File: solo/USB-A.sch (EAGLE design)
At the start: 23 parts, among them U1 USB_TRACES

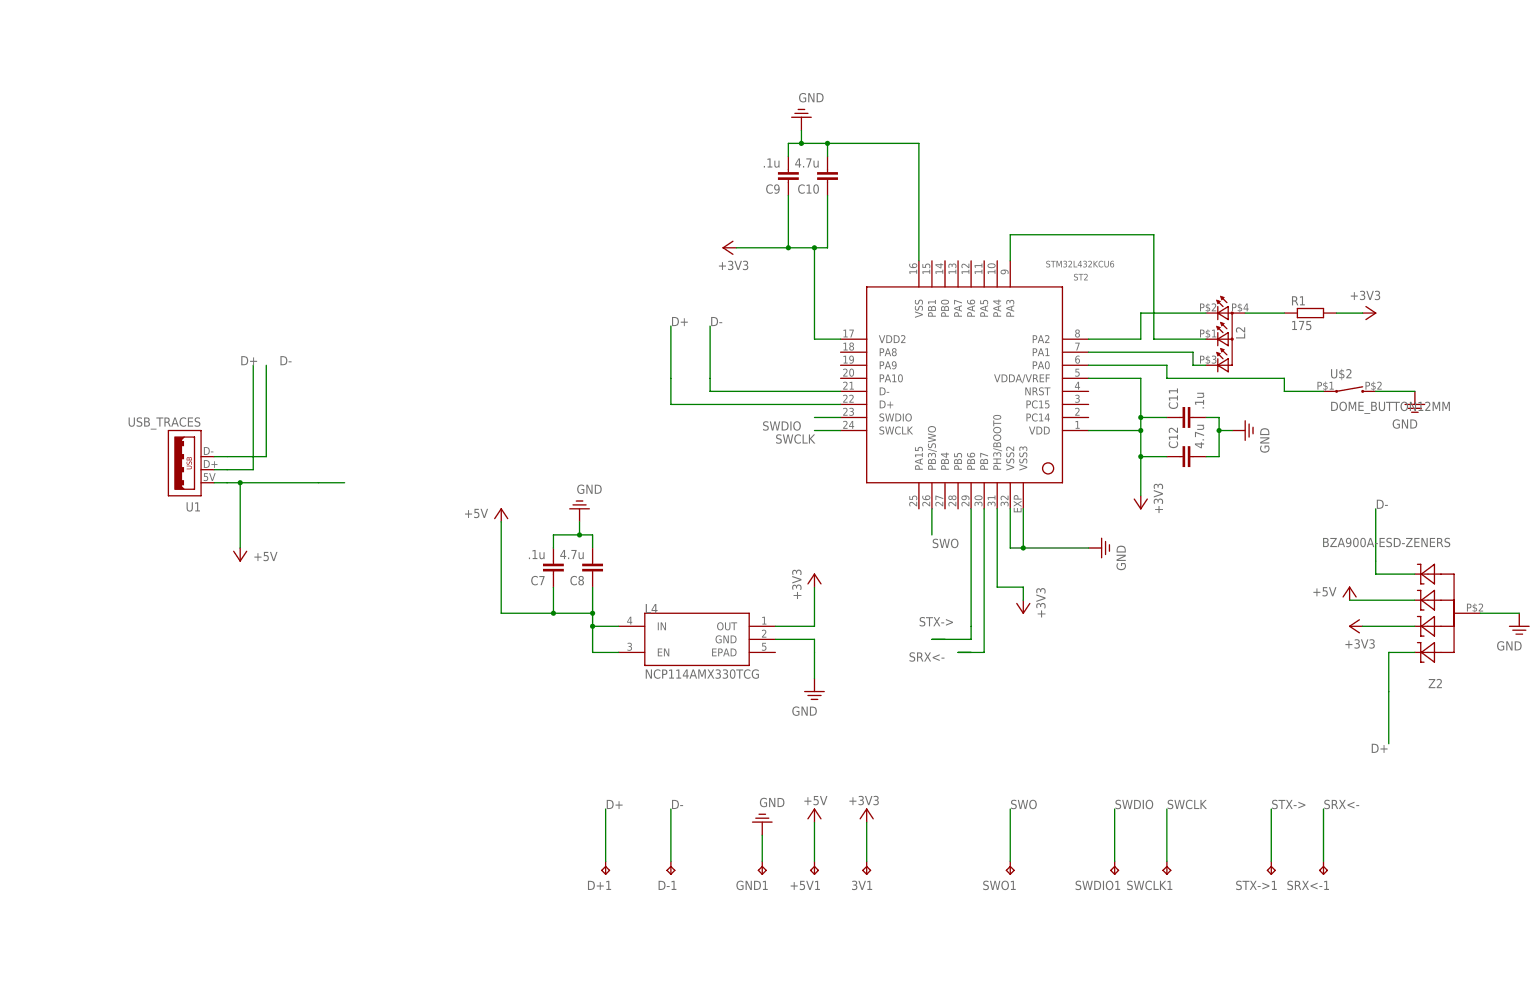
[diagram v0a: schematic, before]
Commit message: fix AMS part footprint :(
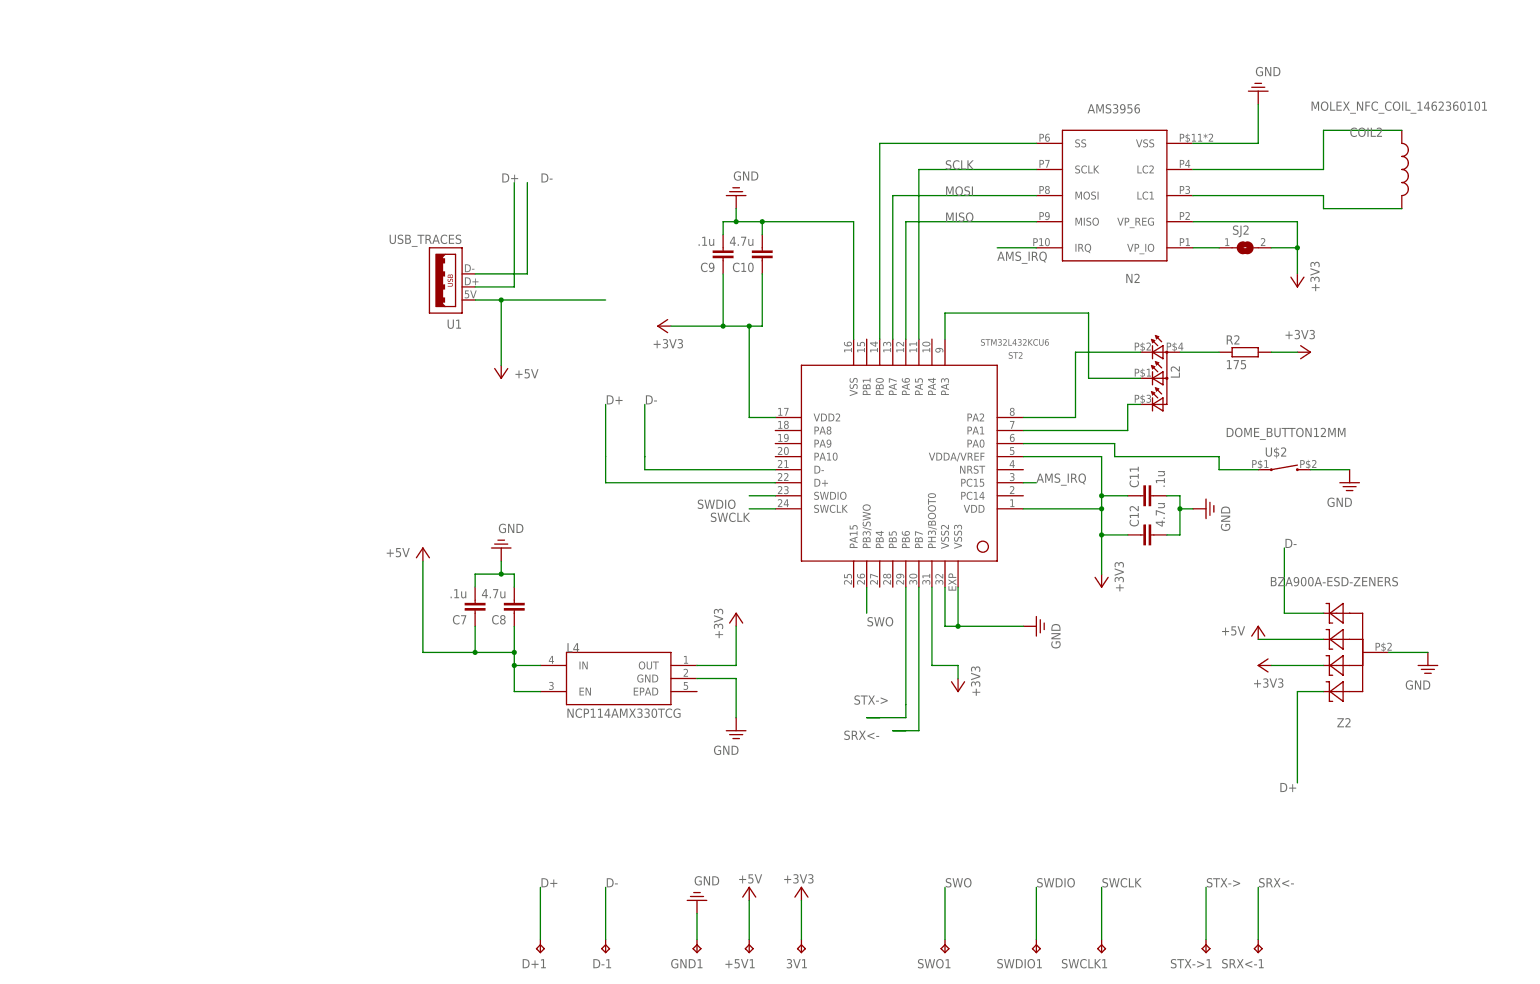
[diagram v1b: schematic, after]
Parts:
- removed R1: 175, efm-fido:RESISTOR
- added COIL2: MOLEX_NFC_COIL_1462360101, efm-fido:MOLEX_NFC_COIL_1462360101
- added N2: AMS3956, efm-fido:AMS3956
- added R2: 175, efm-fido:RESISTOR
- added SJ2: (no value), jumper:SJ
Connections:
- removed net N$7: L2.A2, R1.1
- new net AMS_CS: N2.SS, ST2.PB0
- new net AMS_IRQ: N2.IRQ, ST2.PC15
- new net MISO: N2.MISO, ST2.PA6
- new net MOSI: N2.MOSI, ST2.PA7
- new net N$15: L2.A2, R2.1
- new net N$23: N2.VP_IO, SJ2.1
- new net N$25: COIL2.1, N2.LC2
- new net N$26: COIL2.2, N2.LC1
- new net SCLK: N2.SCLK, ST2.PA5
- net +3V3: now also N2.VP_REG, R2.2, SJ2.2; no longer R1.2
- net PE: now also N2.VSS
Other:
- moved on the sheet: +5V1, 3V1, C10, C11, C12, C7, C8, C9, D+1, D-1, GND1, L2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

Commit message: use hatched footprints, remove bridge
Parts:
- removed SJ2: (no value), jumper:SJ
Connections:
- removed net N$23: N2.VP_IO, SJ2.1
- net +3V3: now also N2.VP_IO; no longer SJ2.2
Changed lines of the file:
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@@
 <part name="+3V14" library="supply1" library_urn="urn:adsk.eagle:library:371" deviceset="+3V3" device=""/>
 <part name="+3V15" library="supply1" library_urn="urn:adsk.eagle:library:371" deviceset="+3V3" device=""/>
-<part name="U$2" library="efm-fido" library_urn="urn:adsk.eagle:library:4245354" deviceset="DOME_BUTTON" device="12MM" package3d_urn="urn:adsk.eagle:package:5648519/5"/>
-<part name="N2" library="efm-fido" library_urn="urn:adsk.eagle:library:4245354" deviceset="AMS3956" device="" package3d_urn="urn:adsk.eagle:package:5825738/3"/>
+<part name="U$2" library="efm-fido" library_urn="urn:adsk.eagle:library:4245354" deviceset="DOME_BUTTON" device="12MM" package3d_urn="urn:adsk.eagle:package:5648519/7"/>
+<part name="N2" library="efm-fido" library_urn="urn:adsk.eagle:library:4245354" deviceset="AMS3956" device="" package3d_urn="urn:adsk.eagle:package:5825738/4"/>
 <part name="SUPPLY18" library="supply2" library_urn="urn:adsk.eagle:library:372" deviceset="PE" device="" value="GND"/>
 <part name="+3V16" library="supply1" library_urn="urn:adsk.eagle:library:371" deviceset="+3V3" device=""/>
-<part name="SJ2" library="jumper" library_urn="urn:adsk.eagle:library:252" deviceset="SJ" device="" package3d_urn="urn:adsk.eagle:package:15471/1"/>
 <part name="COIL2" library="efm-fido" library_urn="urn:adsk.eagle:library:4245354" deviceset="MOLEX_NFC_COIL_1462360101" device="" package3d_urn="urn:adsk.eagle:package:7114966/5"/>
 </parts>
@@
 <instance part="+3V16" gate="G$1" x="292.1" y="134.62" smashed="yes" rot="R180">
 <attribute name="VALUE" x="294.64" y="139.7" size="1.778" layer="96" rot="R270"/>
-</instance>
-<instance part="SJ2" gate="1" x="281.94" y="142.24" smashed="yes">
-<attribute name="NAME" x="279.4" y="144.78" size="1.778" layer="95"/>
-<attribute name="VALUE" x="279.4" y="138.43" size="1.778" layer="96"/>
 </instance>
 <instance part="COIL2" gate="G$1" x="312.42" y="157.48" smashed="yes">
@@
 <pinref part="+3V16" gate="G$1" pin="+3V3"/>
 <wire x1="292.1" y1="137.16" x2="292.1" y2="142.24" width="0.1524" layer="91"/>
-<pinref part="SJ2" gate="1" pin="2"/>
 <wire x1="292.1" y1="142.24" x2="292.1" y2="147.32" width="0.1524" layer="91"/>
-<wire x1="287.02" y1="142.24" x2="292.1" y2="142.24" width="0.1524" layer="91"/>
 <junction x="292.1" y="142.24"/>
+<pinref part="N2" gate="G$1" pin="VP_IO"/>
+<wire x1="271.78" y1="142.24" x2="292.1" y2="142.24" width="0.1524" layer="91"/>
 </segment>
 </net>
@@
 </segment>
 </net>
-<net name="N$23" class="0">
-<segment>
-<pinref part="SJ2" gate="1" pin="1"/>
-<pinref part="N2" gate="G$1" pin="VP_IO"/>
-<wire x1="276.86" y1="142.24" x2="271.78" y2="142.24" width="0.1524" layer="91"/>
-</segment>
-</net>

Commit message: prep for nfc
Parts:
- removed COIL2: MOLEX_NFC_COIL_1462360101, efm-fido:MOLEX_NFC_COIL_1462360101
- added C2, C3, MID: .1u, efm-fido:CAPACITOR
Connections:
- net N$25: now also C2.1, MID.2; no longer COIL2.1
- net N$26: now also C3.2, MID.1; no longer COIL2.2
- net PE: now also C2.2, C3.1
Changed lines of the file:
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@@
 <part name="C12" library="efm-fido" library_urn="urn:adsk.eagle:library:4245354" deviceset="CAPACITOR" device="" package3d_urn="urn:adsk.eagle:package:4245806/7" value="4.7u"/>
 <part name="SUPPLY16" library="supply2" library_urn="urn:adsk.eagle:library:372" deviceset="PE" device="" value="GND"/>
-<part name="ST2" library="efm-fido" library_urn="urn:adsk.eagle:library:4245354" deviceset="STM32L432KCU6" device="" package3d_urn="urn:adsk.eagle:package:4245373/6"/>
+<part name="ST2" library="efm-fido" library_urn="urn:adsk.eagle:library:4245354" deviceset="STM32L432KCU6" device="" package3d_urn="urn:adsk.eagle:package:4245373/7"/>
 <part name="SWO1" library="efm-fido" library_urn="urn:adsk.eagle:library:4245354" deviceset="TEST_POINT" device="" package3d_urn="urn:adsk.eagle:package:4245792/4"/>
 <part name="L4" library="efm-fido" library_urn="urn:adsk.eagle:library:4245354" deviceset="NCP114AMX330TCG" device="" package3d_urn="urn:adsk.eagle:package:5621121/3"/>
@@
 <part name="SUPPLY18" library="supply2" library_urn="urn:adsk.eagle:library:372" deviceset="PE" device="" value="GND"/>
 <part name="+3V16" library="supply1" library_urn="urn:adsk.eagle:library:371" deviceset="+3V3" device=""/>
-<part name="COIL2" library="efm-fido" library_urn="urn:adsk.eagle:library:4245354" deviceset="MOLEX_NFC_COIL_1462360101" device="" package3d_urn="urn:adsk.eagle:package:7114966/5"/>
+<part name="MID" library="efm-fido" library_urn="urn:adsk.eagle:library:4245354" deviceset="CAPACITOR" device="" package3d_urn="urn:adsk.eagle:package:4245806/7" value=".1u"/>
+<part name="C2" library="efm-fido" library_urn="urn:adsk.eagle:library:4245354" deviceset="CAPACITOR" device="" package3d_urn="urn:adsk.eagle:package:4245806/7" value=".1u"/>
+<part name="C3" library="efm-fido" library_urn="urn:adsk.eagle:library:4245354" deviceset="CAPACITOR" device="" package3d_urn="urn:adsk.eagle:package:4245806/7" value=".1u"/>
+<part name="SUPPLY1" library="supply2" library_urn="urn:adsk.eagle:library:372" deviceset="PE" device="" value="GND"/>
+<part name="SUPPLY2" library="supply2" library_urn="urn:adsk.eagle:library:372" deviceset="PE" device="" value="GND"/>
 </parts>
 <sheets>
@@
 <attribute name="VALUE" x="294.64" y="139.7" size="1.778" layer="96" rot="R270"/>
 </instance>
-<instance part="COIL2" gate="G$1" x="312.42" y="157.48" smashed="yes">
-<attribute name="NAME" x="302.26" y="163.83" size="1.778" layer="95"/>
-<attribute name="VALUE" x="294.64" y="168.91" size="1.778" layer="96"/>
+<instance part="MID" gate="G$1" x="314.96" y="157.48" smashed="yes" rot="R180">
+<attribute name="NAME" x="313.436" y="157.099" size="1.778" layer="95" rot="R180"/>
+<attribute name="VALUE" x="313.436" y="162.179" size="1.778" layer="96" rot="R180"/>
+</instance>
+<instance part="C2" gate="G$1" x="314.96" y="172.72" smashed="yes" rot="R180">
+<attribute name="NAME" x="313.436" y="172.339" size="1.778" layer="95" rot="R180"/>
+<attribute name="VALUE" x="313.436" y="177.419" size="1.778" layer="96" rot="R180"/>
+</instance>
+<instance part="C3" gate="G$1" x="317.5" y="142.24" smashed="yes" rot="R180">
+<attribute name="NAME" x="315.976" y="141.859" size="1.778" layer="95" rot="R180"/>
+<attribute name="VALUE" x="315.976" y="146.939" size="1.778" layer="96" rot="R180"/>
+</instance>
+<instance part="SUPPLY1" gate="PE" x="317.5" y="134.62" smashed="yes">
+<attribute name="VALUE" x="313.055" y="129.921" size="1.778" layer="96"/>
+</instance>
+<instance part="SUPPLY2" gate="PE" x="314.96" y="182.88" smashed="yes" rot="R180">
+<attribute name="VALUE" x="319.405" y="187.579" size="1.778" layer="96" rot="R180"/>
 </instance>
 </instances>
@@
 <pinref part="SUPPLY18" gate="PE" pin="PE"/>
 </segment>
+<segment>
+<pinref part="C2" gate="G$1" pin="2"/>
+<pinref part="SUPPLY2" gate="PE" pin="PE"/>
+<wire x1="314.96" y1="177.8" x2="314.96" y2="180.34" width="0.1524" layer="91"/>
+</segment>
+<segment>
+<pinref part="C3" gate="G$1" pin="1"/>
+<pinref part="SUPPLY1" gate="PE" pin="PE"/>
+<wire x1="317.5" y1="139.7" x2="317.5" y2="137.16" width="0.1524" layer="91"/>
+</segment>
 </net>
 <net name="+3V3" class="0">
@@
 <wire x1="271.78" y1="157.48" x2="297.18" y2="157.48" width="0.1524" layer="91"/>
 <wire x1="297.18" y1="157.48" x2="297.18" y2="165.1" width="0.1524" layer="91"/>
-<pinref part="COIL2" gate="G$1" pin="1"/>
-<wire x1="297.18" y1="165.1" x2="312.42" y2="165.1" width="0.1524" layer="91"/>
+<wire x1="297.18" y1="165.1" x2="314.96" y2="165.1" width="0.1524" layer="91"/>
+<pinref part="MID" gate="G$1" pin="2"/>
+<wire x1="314.96" y1="162.56" x2="314.96" y2="165.1" width="0.1524" layer="91"/>
+<pinref part="C2" gate="G$1" pin="1"/>
+<wire x1="314.96" y1="170.18" x2="314.96" y2="165.1" width="0.1524" layer="91"/>
+<junction x="314.96" y="165.1"/>
 </segment>
 </net>
@@
 <wire x1="271.78" y1="152.4" x2="297.18" y2="152.4" width="0.1524" layer="91"/>
 <wire x1="297.18" y1="152.4" x2="297.18" y2="149.86" width="0.1524" layer="91"/>
-<pinref part="COIL2" gate="G$1" pin="2"/>
-<wire x1="297.18" y1="149.86" x2="312.42" y2="149.86" width="0.1524" layer="91"/>
-</segment>
-</net>
+<wire x1="297.18" y1="149.86" x2="314.96" y2="149.86" width="0.1524" layer="91"/>
+<pinref part="MID" gate="G$1" pin="1"/>
+<wire x1="314.96" y1="149.86" x2="314.96" y2="154.94" width="0.1524" layer="91"/>
+<pinref part="C3" gate="G$1" pin="2"/>
+<wire x1="314.96" y1="149.86" x2="314.96" y2="147.32" width="0.1524" layer="91"/>
+<wire x1="314.96" y1="147.32" x2="317.5" y2="147.32" width="0.1524" layer="91"/>
+<junction x="314.96" y="149.86"/>
+</segment>
+</net>
